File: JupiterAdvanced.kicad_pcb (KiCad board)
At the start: 2 copper layers, 220 parts, among them SW1 SW_Push, U1 PRTR5V0U2X, U2 AT90USB1286-AU, Y1 16MHz

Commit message: All diodes placed on PCB (no routes)
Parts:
- removed D31: SOD-123, Diode_SMD:D_SOD-123
- moved D97 365.0 mm to (361.9, 171.4), turned to 90 degrees
- moved D98 359.7 mm to (361.9, 190.5), turned to 90 degrees
- moved D94 358.4 mm to (361.9, 111.8), turned to 90 degrees
- moved D96 354.2 mm to (361.9, 152.4), turned to 90 degrees
- moved D95 349.8 mm to (361.9, 133.3), turned to 90 degrees
- moved D92 337.2 mm to (342.9, 209.6), turned to 90 degrees
- moved D90 336.3 mm to (332.7, 152.4), turned to 90 degrees
- moved D91 335.2 mm to (337.8, 171.4), turned to 90 degrees
- moved D93 334.4 mm to (342.9, 228.6), turned to 90 degrees
- moved D87 314.1 mm to (323.9, 228.6), turned to 90 degrees
- moved D82 299.3 mm to (323.9, 111.8), turned to 90 degrees
- moved D86 297.4 mm to (316.2, 209.6), turned to 90 degrees
- moved D76 290.3 mm to (304.8, 111.8), turned to 90 degrees
- moved D100 289.9 mm to (361.9, 228.6), turned to 90 degrees
- moved D78 285.1 mm to (304.8, 152.4), turned to 90 degrees
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
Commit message: All Diodes moved to B.cu
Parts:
- D1, D10, D100, D11, D12, D13, D14, D15, D16, D17, D18, D19, D2, D20, D21, D22, D23, D24, D25, D26, D27, D28, D29, D3, D30, D32, D33, D34, D35, D36, D37, D38, D39, D4, D40, D41, D42, D43, D44, D45, D46, D47, D48, D49, D5, D50, D51, D52, D53, D54, D55, D56, D57, D58, D59, D6, D60, D61, D62, D63, D64, D65, D66, D67, D68, D69, D7, D70, D71, D72, D73, D74, D75, D76, D77, D78, D79, D8, D80, D81, D82, D83, D84, D85, D86, D87, D88, D89, D9, D90, D91, D92, D93, D94, D95, D96, D97, D98, D99: moved to B.Cu

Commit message: Design Notes.txt added
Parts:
- moved C4 21.1 mm to (221.2, 55.6)
- moved U1 21.1 mm to (230.5, 49.5)
- moved SW1 21.1 mm to (120.1, 51.3)
- moved USB1 21.1 mm to (110.0, 57.2)
- moved R1 21.1 mm to (210.4, 61.9)
- moved R8 21.1 mm to (195.0, 38.1)
- moved C1 21.1 mm to (214.8, 63.0)
- moved C2 21.1 mm to (226.3, 51.9)
- moved C3 21.1 mm to (221.9, 52.3)
- moved C5 21.1 mm to (214.8, 60.1)
- moved C6 21.1 mm to (225.1, 48.9)
- moved C7 21.1 mm to (204.6, 63.0)
- moved F11 21.1 mm to (211.0, 55.8)
- moved R2 21.1 mm to (210.4, 58.9)
- moved R3 21.1 mm to (195.0, 23.4)
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
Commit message: LastOfDay - Cutout and Switch alignment still unfinished.
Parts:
- C1, C2, C3, C4, C5, C6, C7, F11, R1, R2, R3, R4, R5, R6, R7, R8, SW1, U1, U2, USB1, Y1: moved to B.Cu
- moved C5 61.9 mm to (267.3, 27.3), turned to 90 degrees
- moved R3 59.1 mm to (154.1, 66.1)
- moved R4 55.0 mm to (154.1, 63.1)
- moved Y1 54.1 mm to (262.1, 27.3), turned to 180 degrees
- moved R1 53.3 mm to (169.5, 27.6)
- moved R5 51.2 mm to (154.1, 60.2)
- moved R8 50.7 mm to (245.2, 31.5), turned to 270 degrees
- moved R2 49.7 mm to (169.5, 30.6)
- moved R6 47.9 mm to (154.1, 57.2)
- moved USB1 47.8 mm to (69.2, 32.3)
- moved F11 46.4 mm to (170.1, 33.7)
- moved C1 45.8 mm to (259.4, 52.8), turned to 180 degrees
- moved SW1 42.9 mm to (79.3, 38.2)
- moved U1 41.9 mm to (189.7, 40.0)
- moved C6 38.3 mm to (256.7, 27.3), turned to 270 degrees
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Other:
- board outline added: 314.8 x 162.9 mm

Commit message: All cutouts, switch locations and diodes aligned
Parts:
- moved D76 4.86 mm to (307.9, 106.9)
- moved MXSp10 4.86 mm to (284.7, 100.8)
- moved MXSp13 4.86 mm to (341.7, 100.8)
- moved D38 4.86 mm to (193.6, 106.9)
- moved MXSp3 4.86 mm to (132.2, 100.8)
- moved MXSp8 4.86 mm to (227.4, 100.8)
- moved D7 4.86 mm to (98.3, 107.0)
- moved MXSp1 4.86 mm to (94.1, 100.8)
- moved MXSp2 4.86 mm to (113.1, 100.8)
- moved D1 4.86 mm to (79.3, 106.9)
- moved D12 4.86 mm to (117.4, 106.9)
- moved D18 4.86 mm to (136.4, 106.9)
- moved D25 4.86 mm to (155.5, 106.9)
- moved D32 4.86 mm to (174.5, 106.9)
- moved D45 4.86 mm to (212.6, 106.9)
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
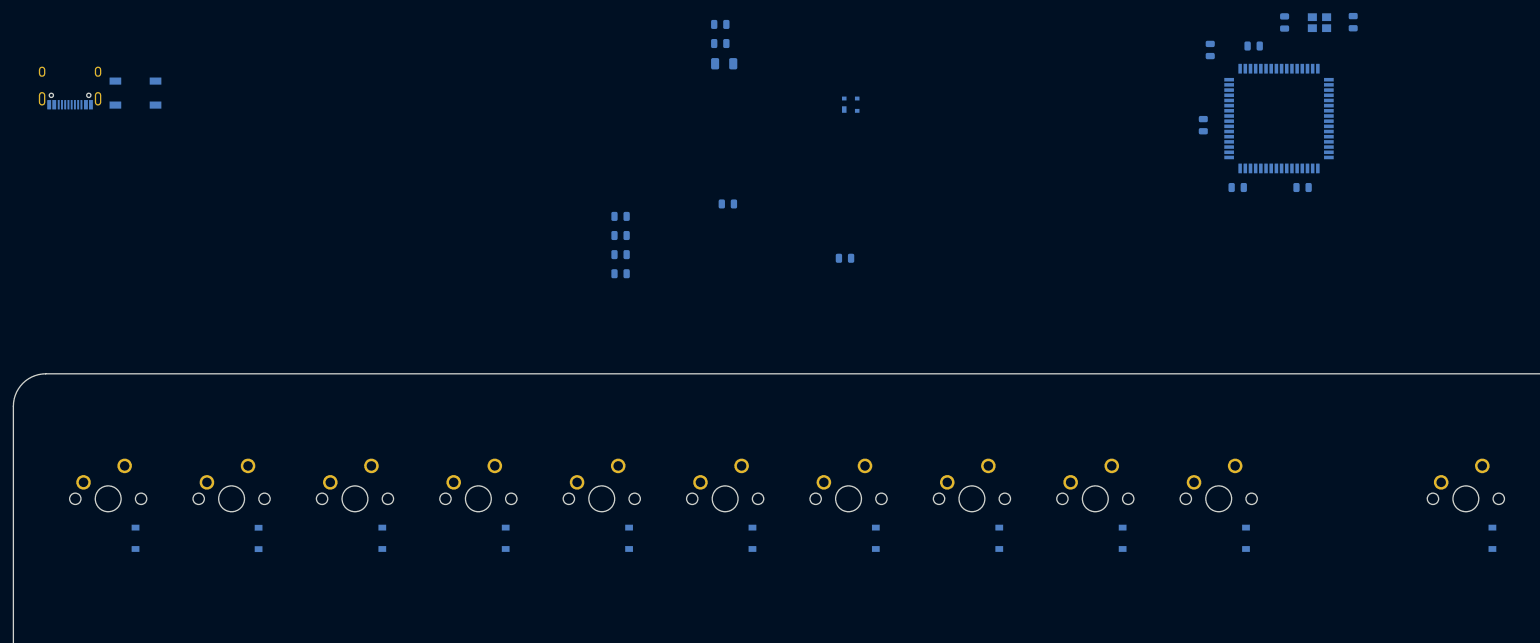
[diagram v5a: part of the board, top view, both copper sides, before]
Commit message: Cleaned up USB C connector resistors
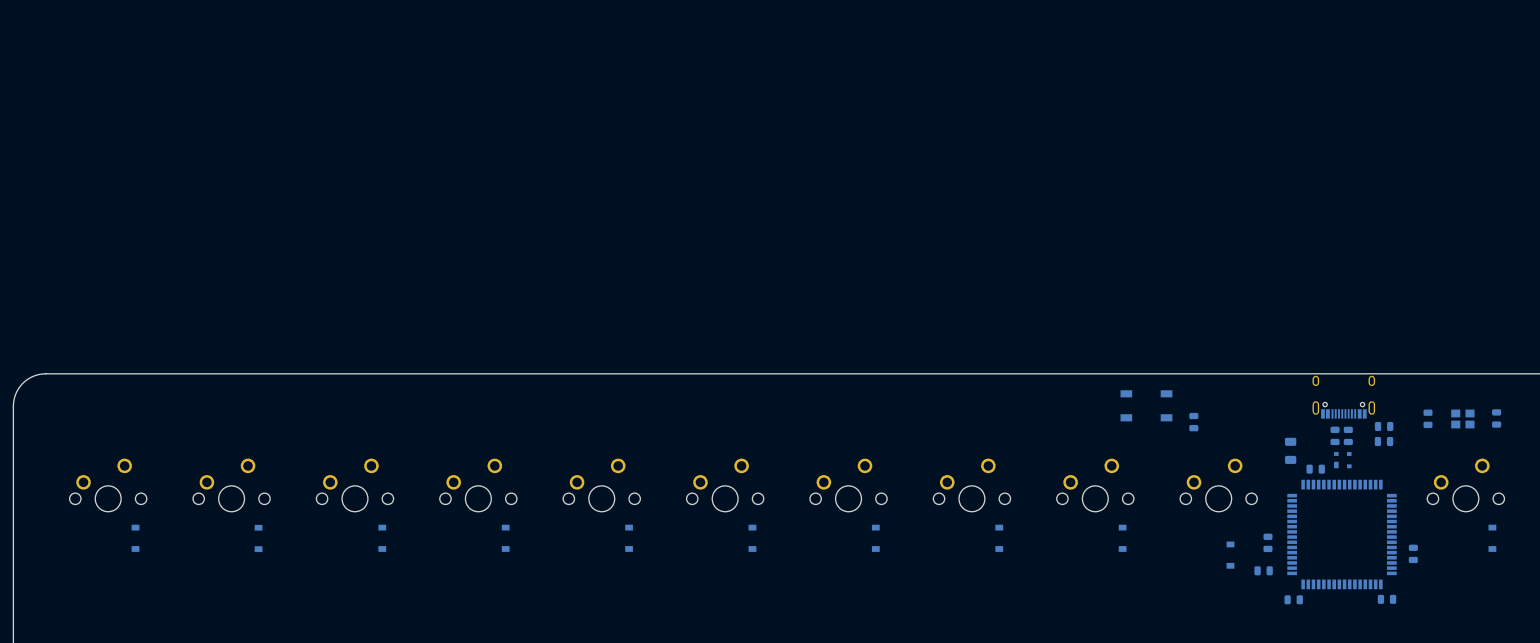
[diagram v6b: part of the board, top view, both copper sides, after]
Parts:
- removed R5, R6: 22, Resistor_SMD:R_0805_2012Metric
- moved USB1 202.4 mm to (265.8, 80.0)
- moved SW1 163.4 mm to (235.3, 86.5)
- moved R3 120.7 mm to (272.0, 92.0)
- moved R1 119.8 mm to (272.0, 89.7)
- moved R7 118.8 mm to (276.5, 109.3), turned to 270 degrees
- moved R4 115.8 mm to (266.5, 91.1), turned to 270 degrees
- moved R2 112.6 mm to (264.5, 91.1), turned to 270 degrees
- moved F11 105.9 mm to (257.6, 93.4), turned to 270 degrees
- moved U1 93.7 mm to (265.7, 94.9)
- moved C7 80.7 mm to (253.4, 112.0)
- moved C2 66.0 mm to (261.5, 96.3)
- moved C3 65.3 mm to (254.1, 107.6)
- moved C5 65.1 mm to (289.4, 88.4)
- moved C6 65.1 mm to (278.8, 88.5)
- moved Y1 65.1 mm to (284.2, 88.5)
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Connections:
- U2 pad 4: Net-(R5-Pad1) -> D-
- U2 pad 5: Net-(R6-Pad1) -> D+
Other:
- net class Default: trace_width 0.25 -> 0.254
- net class Power added: clearance 0.2, trace_width 0.381, via_dia 0.8, via_drill 0.4

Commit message: Columns Routed. Working on the USB C connector routing.
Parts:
- added R5: 22, Resistor_SMD:R_0805_2012Metric, B.Cu at (264.7, 97.7)
- added R6: 22, Resistor_SMD:R_0805_2012Metric, B.Cu at (267.0, 97.7)
- Pipe1: footprint MX_Only:MXOnly-1.5U-NoLED -> MX_Only:MXOnly-1U-NoLED
- moved C5 25.3 mm to (284.6, 113.3), turned to 270 degrees
- moved Y1 25.3 mm to (279.0, 113.3), turned to 0 degrees
- moved C6 25.1 mm to (282.5, 113.3)
- moved C1 18.0 mm to (255.0, 112.0), turned to 270 degrees
- moved C2 17.5 mm to (276.1, 105.7), turned to 270 degrees
- moved R7 16.7 mm to (262.9, 118.9), turned to 180 degrees
- moved C4 16.6 mm to (255.0, 100.1), turned to 180 degrees
- moved C7 15.4 mm to (257.4, 97.1)
- moved R3 6.27 mm to (274.1, 86.1)
- moved R1 6.06 mm to (274.1, 84.0)
- moved F11 4.34 mm to (261.3, 95.7), turned to 90 degrees
- moved C3 4.09 mm to (254.9, 103.6)
- moved U2 2.33 mm to (265.7, 108.7), turned to 270 degrees
- moved R2 2.30 mm to (262.2, 91.1), turned to 180 degrees
- moved R4 1.52 mm to (268.0, 91.1), turned to 0 degrees
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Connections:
- net Net-(R2-Pad2) renamed DN
- net Net-(R4-Pad2) renamed DP
- U2 pad 17: Net-(U2-Pad17) -> COL11
- U2 pad 18: Net-(U2-Pad18) -> COL12
- U2 pad 19: Net-(U2-Pad19) -> COL13
- U2 pad 25: Net-(U2-Pad25) -> COL14
- U2 pad 26: Net-(U2-Pad26) -> COL15
- U2 pad 33: Net-(U2-Pad33) -> COL10
- U2 pad 34: Net-(U2-Pad34) -> ROW0
- U2 pad 35: Net-(U2-Pad35) -> ROW1
- U2 pad 36: Net-(U2-Pad36) -> ROW2
- U2 pad 37: Net-(U2-Pad37) -> COL3
- U2 pad 38: Net-(U2-Pad38) -> ROW4
- U2 pad 39: Net-(U2-Pad39) -> ROW5
- U2 pad 4: D- -> Net-(R6-Pad1)
- U2 pad 40: Net-(U2-Pad40) -> ROW6
- U2 pad 49: Net-(U2-Pad49) -> COL9
- U2 pad 5: D+ -> Net-(R5-Pad1)
- U2 pad 50: Net-(U2-Pad50) -> COL8
- U2 pad 51: Net-(U2-Pad51) -> COL7
- U2 pad 54: Net-(U2-Pad54) -> COL6
- U2 pad 55: Net-(U2-Pad55) -> COL5
- U2 pad 56: Net-(U2-Pad56) -> COL5
- U2 pad 57: Net-(U2-Pad57) -> COL4
- U2 pad 58: Net-(U2-Pad58) -> COL3
- U2 pad 59: Net-(U2-Pad59) -> COL2
- U2 pad 60: Net-(U2-Pad60) -> COL1
- U2 pad 61: Net-(U2-Pad61) -> COL0
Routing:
- net COL13: track 0.00 -> 148.1 mm
- net COL3: track 0.00 -> 138.6 mm
- net COL1: track 0.00 -> 137.1 mm
- net COL11: track 0.00 -> 135.7 mm
- net COL6: track 0.00 -> 134.7 mm
- net COL14: track 0.00 -> 131.9 mm
- net COL12: track 0.00 -> 131.8 mm
- net COL0: track 0.00 -> 129.1 mm
- net COL15: track 0.00 -> 123.8 mm
- net COL2: track 0.00 -> 114.7 mm
- net COL7: track 0.00 -> 114.6 mm
- net COL5: track 0.00 -> 114.6 mm
- net COL9: track 0.00 -> 114.6 mm
- net COL8: track 0.00 -> 114.6 mm
- net COL4: track 0.00 -> 114.6 mm
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
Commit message: Routing work
USB connector and pairs routed. Rows 1-6 complete. Row 0 still needs work
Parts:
- removed R2, R4: 22, Resistor_SMD:R_0805_2012Metric
- moved F11 10.2 mm to (271.6, 95.6)
- moved R6 5.77 mm to (261.3, 97.7)
- moved U1 3.16 mm to (262.5, 92.3), turned to 180 degrees
- moved USB1 2.56 mm to (262.6, 80.7)
- moved C7 1.93 mm to (256.6, 95.3)
- moved R5 0.95 mm to (263.8, 97.7)
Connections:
- R5 pad 1: Net-(R5-Pad1) -> DP
- R6 pad 1: Net-(R6-Pad1) -> DN
- U2 pad 4: Net-(R6-Pad1) -> DN
- U2 pad 5: Net-(R5-Pad1) -> DP
- USB1 pad 5: DN -> D-
- USB1 pad 6: DP -> D+
- USB1 pad 7: DN -> D-
- USB1 pad 8: DP -> D+
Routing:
- net ROW2: track 0.00 -> 288.3 mm
- net ROW6: track 0.00 -> 285.8 mm
- net ROW1: track 0.00 -> 285.8 mm
- net COL3: track 138.6 -> 421.2 mm
- net ROW4: track 0.00 -> 282.0 mm
- net ROW5: track 0.00 -> 256.6 mm
- net ROW0: track 0.00 -> 246.4 mm
- net D+: track 0.00 -> 12.8 mm
- net Net-(D57-Pad2): track 0.00 -> 12.4 mm
- net D-: track 0.00 -> 11.2 mm
- net Net-(D7-Pad2): track 0.00 -> 10.2 mm
- net Net-(D94-Pad2): track 0.00 -> 10.2 mm
- net Net-(D88-Pad2): track 0.00 -> 10.2 mm
- net Net-(D82-Pad2): track 0.00 -> 10.2 mm
- net Net-(D76-Pad2): track 0.00 -> 10.2 mm
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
